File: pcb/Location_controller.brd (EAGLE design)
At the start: 75 x 48 mm, 59 parts, among them IC1 LIS302DL

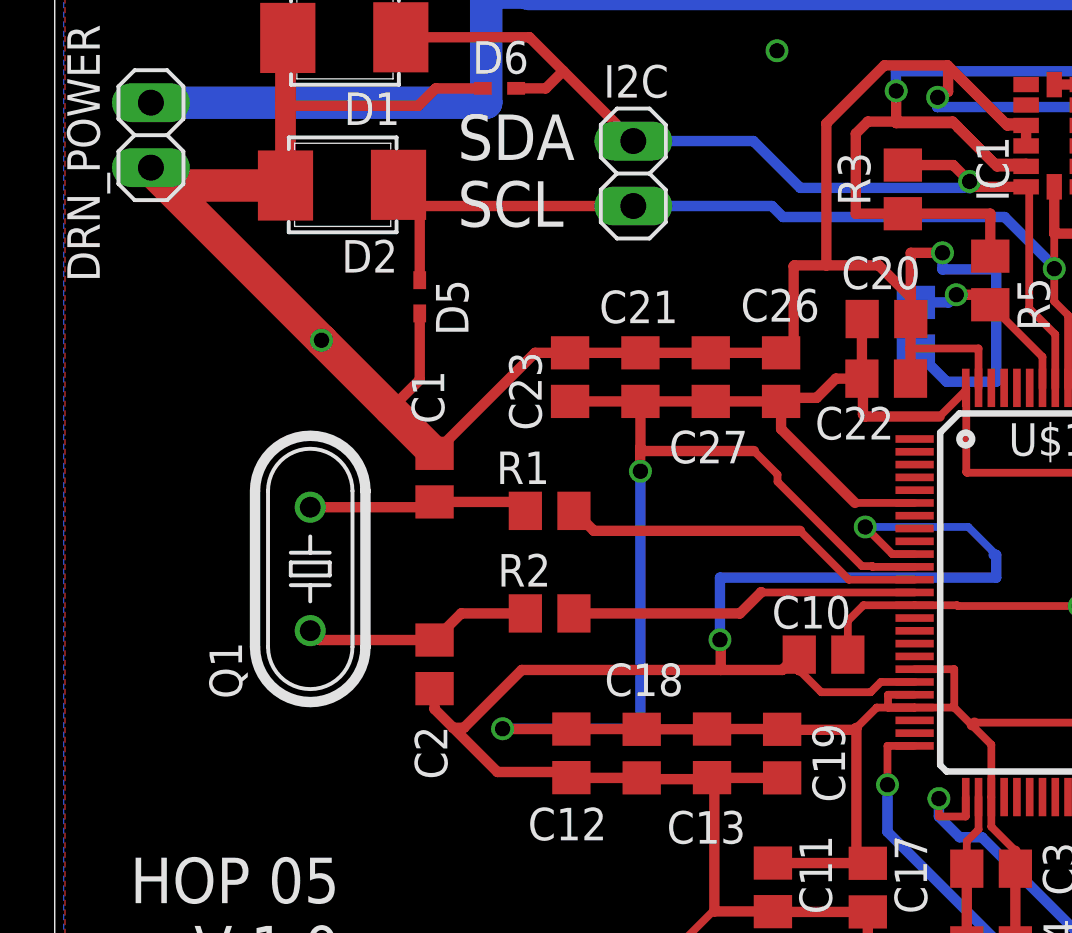
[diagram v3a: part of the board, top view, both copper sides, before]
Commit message: Move crystal closer to microcontroller
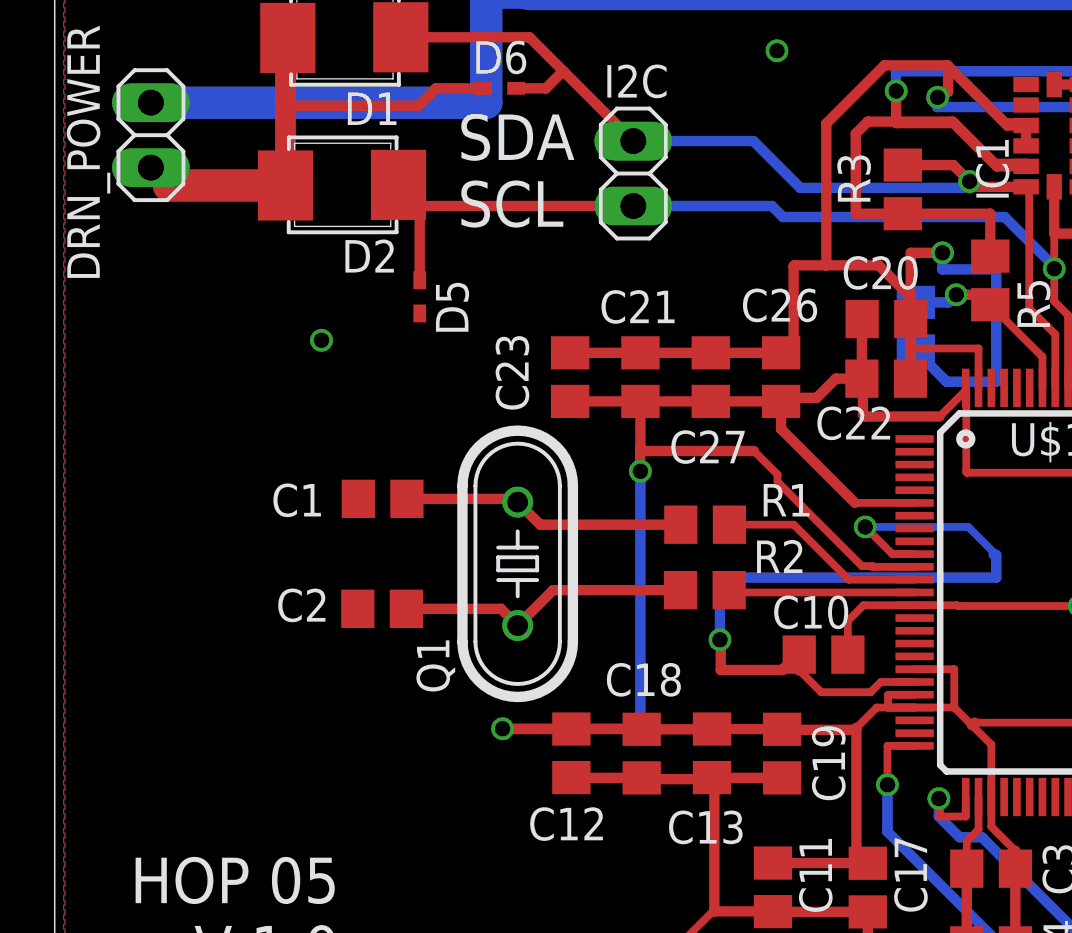
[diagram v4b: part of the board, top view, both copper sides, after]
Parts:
- moved Q1 8.11 mm to (18.1, 23.9)
- moved R2 6.14 mm to (25.4, 22.9)
- moved R1 6.10 mm to (25.4, 25.5)
- moved C2 2.99 mm to (12.8, 22.2), turned to 180 degrees
- moved C1 2.19 mm to (12.8, 26.5), turned to 180 degrees
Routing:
- net GND: track 391.5 -> 346.4 mm
- net OSC_OUT: track 13.7 -> 7.29 mm
- net OSC_IN: track 14.4 -> 8.13 mm
- net N$1: track 8.99 -> 11.6 mm
- net N$2: track 8.64 -> 11.1 mm

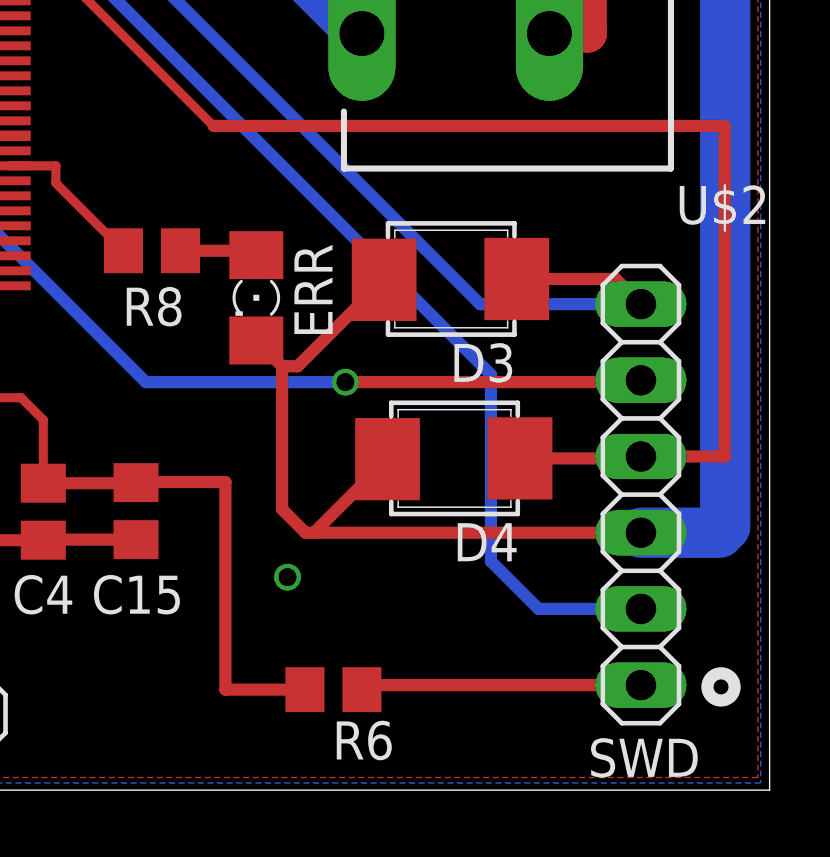
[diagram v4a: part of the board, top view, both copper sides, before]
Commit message: Add TVS to programmer pins
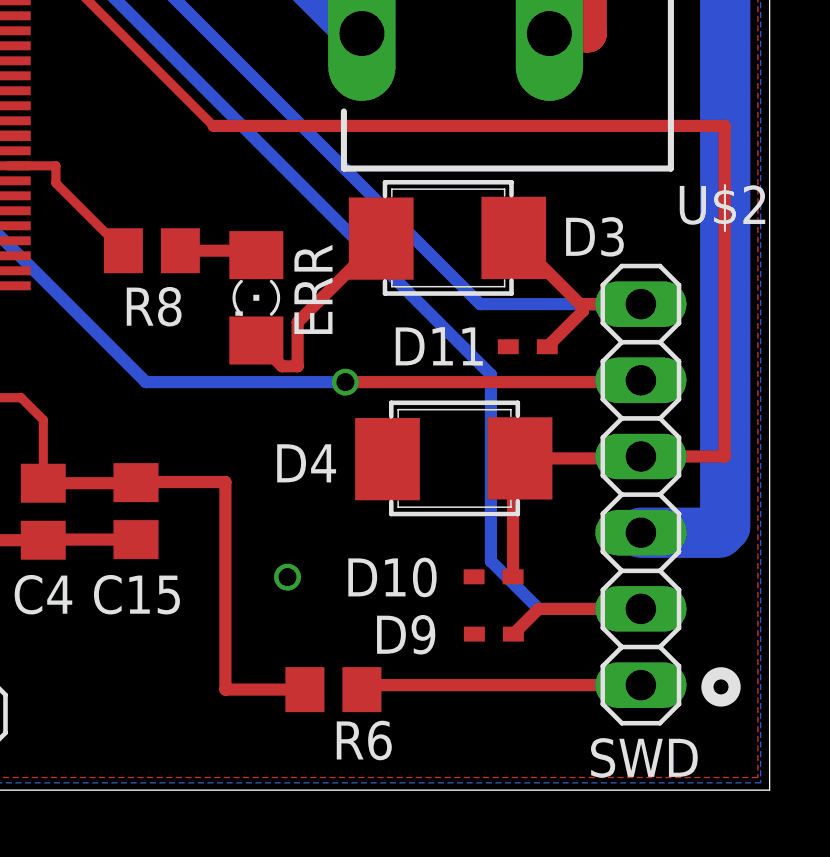
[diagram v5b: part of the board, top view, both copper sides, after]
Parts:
- added D10, D11, D9: (no value), diode:SOD523
- moved D3 1.37 mm to (64.2, 18.3)
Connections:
- net GND: now also D10.A, D11.A, D9.A
- net SWCLK: now also D9.C
- net SWDIO: now also D10.C
- net SWO: now also D11.C
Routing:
- net GND: track 346.4 -> 327.2 mm
- net SWCLK: track 38.2 -> 42.8 mm
- net SWDIO: track 43.9 -> 47.9 mm
- net SWO: track 45.0 -> 47.6 mm
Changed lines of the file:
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@@
 <attribute name="SPICEPREFIX" value="R" x="33.67" y="33.2" size="1.778" layer="28" rot="MR270" display="off"/>
 </element>
-<element name="D4" library="stm32f4" package="SMB" value="ZDIODE" x="64.37" y="10.93" rot="R180"/>
-<element name="D3" library="stm32f4" package="SMB" value="ZDIODE" x="64.26" y="16.91" rot="R180"/>
+<element name="D4" library="stm32f4" package="SMB" value="ZDIODE" x="64.37" y="10.93" smashed="yes" rot="R180">
+<attribute name="NAME" x="60.636" y="11.528" size="1.27" layer="25" ratio="10" rot="R180"/>
+<attribute name="VALUE" x="66.656" y="14.5114" size="1.27" layer="27" ratio="10" rot="R180"/>
+</element>
+<element name="D3" library="stm32f4" package="SMB" value="ZDIODE" x="64.16" y="18.28" smashed="yes" rot="R180">
+<attribute name="NAME" x="70.266" y="19.078" size="1.27" layer="25" ratio="10" rot="R180"/>
+<attribute name="VALUE" x="66.446" y="21.8614" size="1.27" layer="27" ratio="10" rot="R180"/>
+</element>
 <element name="D5" library="diode" package="SOD523" value="" x="14.27" y="34.42" rot="R270"/>
 <element name="D6" library="diode" package="SOD523" value="" x="17.44" y="42.52" smashed="yes" rot="R180">
@@
 <element name="D7" library="diode" package="SOD523" value="" x="42.04" y="5.92" rot="R90"/>
 <element name="D8" library="diode" package="SOD523" value="" x="44.93" y="5.96" rot="R90"/>
+<element name="D9" library="diode" package="SOD523" value="" x="65.86" y="5.2" smashed="yes" rot="R180">
+<attribute name="NAME" x="63.965" y="5.815" size="1.27" layer="25" rot="R180"/>
+<attribute name="VALUE" x="66.495" y="7.105" size="1.27" layer="27" rot="R180"/>
+</element>
+<element name="D10" library="diode" package="SOD523" value="" x="65.85" y="7.11" smashed="yes" rot="R180">
+<attribute name="NAME" x="64.005" y="7.725" size="1.27" layer="25" rot="R180"/>
+<attribute name="VALUE" x="66.485" y="9.015" size="1.27" layer="27" rot="R180"/>
+</element>
+<element name="D11" library="diode" package="SOD523" value="" x="66.99" y="14.78" smashed="yes" rot="R180">
+<attribute name="NAME" x="65.585" y="15.425" size="1.27" layer="25" rot="R180"/>
+<attribute name="VALUE" x="67.625" y="16.685" size="1.27" layer="27" rot="R180"/>
+</element>
 </elements>
 <signals>
@@
 <wire x1="72.75" y1="37.47" x2="71.14" y2="39.08" width="1.6764" layer="1"/>
 <wire x1="57.89" y1="14.988" x2="58.75" y2="14.128" width="0.4064" layer="1"/>
-<wire x1="58.75" y1="14.128" x2="58.75" y2="9.36" width="0.4064" layer="1"/>
-<wire x1="58.75" y1="9.36" x2="59.53" y2="8.58" width="0.4064" layer="1"/>
-<wire x1="59.8102" y1="8.58" x2="70.71" y2="8.58" width="0.4064" layer="1"/>
 <contactref element="D1" pad="2"/>
 <contactref element="D2" pad="2"/>
@@
 <contactref element="D3" pad="2"/>
 <wire x1="72.75" y1="33.57" x2="72.75" y2="37.47" width="1.6764" layer="1"/>
-<wire x1="59.53" y1="8.58" x2="59.8102" y2="8.58" width="0.4064" layer="1"/>
-<wire x1="59.8102" y1="8.58" x2="62.2618" y2="11.0316" width="0.4064" layer="1"/>
 <wire x1="58.75" y1="14.128" x2="59.2682" y2="14.128" width="0.4064" layer="1"/>
-<wire x1="59.2682" y1="14.128" x2="62.1518" y2="17.0116" width="0.4064" layer="1"/>
 <wire x1="59.32" y1="42.24" x2="55.69" y2="38.61" width="1.27" layer="1"/>
 <wire x1="65.41" y1="42.24" x2="65.41" y2="38.73" width="1.27" layer="1"/>
@@
 <via x="28.24" y="43.99" extent="1-16" drill="0.6" shape="square"/>
 <via x="58.93" y="7.1" extent="1-16" drill="0.6" shape="square"/>
+<contactref element="D9" pad="A"/>
+<contactref element="D10" pad="A"/>
+<contactref element="D11" pad="A"/>
+<wire x1="59.2682" y1="14.128" x2="59.2682" y2="15.598" width="0.4064" layer="1"/>
+<wire x1="59.2682" y1="15.598" x2="62.0518" y2="18.3816" width="0.4064" layer="1"/>
 </signal>
 <signal name="N$1">
@@
 <wire x1="48.73" y1="31.42" x2="47.62" y2="31.42" width="0.3048" layer="1"/>
 <wire x1="47.62" y1="31.42" x2="47.62" y2="30.81" width="0.3048" layer="1"/>
+<contactref element="D9" pad="C"/>
+<wire x1="66.46" y1="5.2" x2="67.3" y2="6.04" width="0.4064" layer="1"/>
+<wire x1="67.3" y1="6.04" x2="70.71" y2="6.04" width="0.4064" layer="1"/>
 </signal>
 <signal name="SWO">
@@
 <wire x1="49.8" y1="31.75" x2="65.35" y2="16.2" width="0.4064" layer="16"/>
 <contactref element="D3" pad="1"/>
-<wire x1="66.5714" y1="17.037" x2="69.873" y2="17.037" width="0.4064" layer="1"/>
-<wire x1="69.873" y1="17.037" x2="70.71" y2="16.2" width="0.4064" layer="1"/>
+<contactref element="D11" pad="C"/>
+<wire x1="66.4714" y1="18.407" x2="68.6784" y2="16.2" width="0.4064" layer="1"/>
+<wire x1="68.6784" y1="16.2" x2="68.78" y2="16.2" width="0.4064" layer="1"/>
+<wire x1="68.78" y1="16.2" x2="70.71" y2="16.2" width="0.4064" layer="1"/>
+<wire x1="67.59" y1="14.78" x2="68.78" y2="15.97" width="0.4064" layer="1"/>
+<wire x1="68.78" y1="15.97" x2="68.78" y2="16.2" width="0.4064" layer="1"/>
 </signal>
 <signal name="NRST">
@@
 <wire x1="66.6814" y1="11.057" x2="70.647" y2="11.057" width="0.4064" layer="1"/>
 <wire x1="70.647" y1="11.057" x2="70.71" y2="11.12" width="0.4064" layer="1"/>
+<contactref element="D10" pad="C"/>
+<wire x1="66.6814" y1="11.057" x2="66.45" y2="10.8256" width="0.4064" layer="1"/>
+<wire x1="66.45" y1="10.8256" x2="66.45" y2="7.11" width="0.4064" layer="1"/>
 </signal>
 <signal name="N$5">

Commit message: Swap power plug for correct dimensions
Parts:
- U$2: value DCBARRELPTH -> 2.1MMJACKTHM; device BaseApp:DCJACK_2MM_PTH -> adafruit:PJ-102A
- moved U$2 4.71 mm to (70.6, 26.9), turned to 270 degrees
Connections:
- removed net GNDBREAK: U$2.GNDBREAK
- net GND: now also U$2.RING; no longer U$2.GND
- net N$5: now also U$2.TIP; no longer U$2.PWR
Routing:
- net GND: track 327.2 -> 294.1 mm
- net N$5: track 21.2 -> 20.5 mm
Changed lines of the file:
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@@
 <layer number="132" name="bAdjust" color="7" fill="1" visible="no" active="yes"/>
 <layer number="144" name="Drill_legend" color="7" fill="1" visible="no" active="yes"/>
+<layer number="150" name="Notes" color="7" fill="1" visible="no" active="yes"/>
 <layer number="151" name="HeatSink" color="7" fill="1" visible="no" active="yes"/>
 <layer number="152" name="_bDocu" color="7" fill="1" visible="no" active="yes"/>
+<layer number="153" name="FabDoc1" color="6" fill="1" visible="no" active="no"/>
+<layer number="154" name="FabDoc2" color="2" fill="1" visible="no" active="no"/>
+<layer number="155" name="FabDoc3" color="7" fill="15" visible="no" active="no"/>
 <layer number="199" name="Contour" color="7" fill="1" visible="no" active="yes"/>
 <layer number="200" name="200bmp" color="1" fill="10" visible="no" active="no"/>
@@
 <attribute name="VALUE" x="74.315" y="37.81" size="1.27" layer="27" rot="R90"/>
 </element>
-<element name="U$2" library="BaseApp" package="DCJACK_2MM_PTH" value="DCBARRELPTH" x="75.01" y="25.22" rot="R90"/>
+<element name="U$2" library="adafruit" package="PJ-102A" value="2.1MMJACKTHM" x="70.62" y="26.92" rot="R270"/>
 <element name="JP1" library="pinhead" package="1X06" value="" x="41.91" y="2.54"/>
 <element name="JP2" library="pinhead" package="1X06" value="" x="25.4" y="2.54"/>
@@
 <wire x1="50.04" y1="33.53" x2="50.04" y2="33.55" width="0.4064" layer="1"/>
 <wire x1="50.04" y1="33.55" x2="49.28" y2="34.31" width="0.4064" layer="1"/>
-<contactref element="U$2" pad="GND"/>
-<contactref element="U$2" pad="GND"/>
-<wire x1="68.94" y1="25.22" x2="67.66" y2="25.22" width="1.27" layer="1"/>
+<contactref element="U$2" pad="RING"/>
+<contactref element="U$2" pad="RING"/>
 <wire x1="44.28" y1="40.53" x2="44.28" y2="41.07" width="0.4064" layer="1"/>
 <wire x1="44.28" y1="41.07" x2="42.55" y2="41.07" width="0.4064" layer="1"/>
@@
 <contactref element="PWR" pad="C"/>
 <contactref element="ERR" pad="C"/>
-<wire x1="72.75" y1="37.47" x2="71.14" y2="39.08" width="1.6764" layer="1"/>
 <wire x1="57.89" y1="14.988" x2="58.75" y2="14.128" width="0.4064" layer="1"/>
 <contactref element="D1" pad="2"/>
@@
 <wire x1="34.87" y1="31.05" x2="36.81" y2="31.05" width="0.4064" layer="16"/>
 <wire x1="70.27" y1="33.298" x2="70.442" y2="33.47" width="1.016" layer="1"/>
-<wire x1="72.65" y1="33.47" x2="72.75" y2="33.57" width="1.016" layer="1"/>
 <contactref element="D4" pad="2"/>
 <contactref element="D3" pad="2"/>
-<wire x1="72.75" y1="33.57" x2="72.75" y2="37.47" width="1.6764" layer="1"/>
 <wire x1="58.75" y1="14.128" x2="59.2682" y2="14.128" width="0.4064" layer="1"/>
 <wire x1="59.32" y1="42.24" x2="55.69" y2="38.61" width="1.27" layer="1"/>
@@
 <wire x1="71.14" y1="39.08" x2="65.41" y2="39.08" width="1.27" layer="1"/>
 <wire x1="65.41" y1="39.08" x2="65.41" y2="38.73" width="1.27" layer="1"/>
-<wire x1="55.66" y1="32.22" x2="68.91" y2="32.22" width="1.27" layer="1"/>
-<wire x1="68.94" y1="32.22" x2="68.97" y2="32.22" width="1.27" layer="1"/>
-<wire x1="70.27" y1="33.298" x2="72.75" y2="33.298" width="1.6764" layer="1"/>
-<wire x1="72.75" y1="33.298" x2="72.75" y2="33.57" width="1.6764" layer="1"/>
-<wire x1="70.27" y1="33.298" x2="68.91" y2="33.298" width="1.27" layer="1"/>
-<wire x1="68.91" y1="33.298" x2="68.91" y2="32.22" width="1.27" layer="1"/>
-<wire x1="68.91" y1="32.22" x2="68.94" y2="32.22" width="1.27" layer="1"/>
-<wire x1="68.94" y1="32.22" x2="68.94" y2="25.22" width="1.27" layer="1"/>
 <contactref element="D6" pad="A"/>
 <contactref element="D5" pad="A"/>
@@
 <signal name="N$5">
 <contactref element="POWER" pad="1"/>
-<contactref element="U$2" pad="PWR"/>
+<contactref element="U$2" pad="TIP"/>
 <wire x1="49.38" y1="41.43" x2="49.38" y2="37.25" width="1.6764" layer="16"/>
-<wire x1="49.38" y1="37.25" x2="61.41" y2="25.22" width="1.6764" layer="16"/>
+<wire x1="49.38" y1="37.25" x2="59.81" y2="26.82" width="1.6764" layer="16"/>
+<wire x1="59.81" y1="26.82" x2="61.33" y2="26.82" width="1.6764" layer="16"/>
 </signal>
 <signal name="IN_3V">
@@
 </signal>
 <signal name="GNDBREAK">
-<contactref element="U$2" pad="GNDBREAK"/>
 </signal>
 <signal name="N$12">
